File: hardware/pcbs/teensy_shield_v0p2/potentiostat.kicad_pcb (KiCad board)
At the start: 2 copper layers, 144.8 x 88.9 mm, 28 parts, among them K1 CONN_3, P1 CONN_2, P10 CONN_2, P11 CONN_2, P12 CONN_2, P13 CONN_5X2, P14 CONN_5X2, P15 CONN_2X2, P16 CONN_2X2, P17 CONN_2, P18 CONN_2, P19 CONN_2, P2 CONN_2, P20 CONN_2, P21 CONN_2, P3 CONN_2, P4 CONN_2, P5 CONN_2, P6 CONN_2, P7 CONN_2, P8 CONN_2, P9 CONN_2, U2 TEENSY3.1, U6 MEA1D05XXSC

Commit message: Work on layout of teensy pcb version 0.2
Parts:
- added C1: 4.7uF, Capacitor_SMD:C_0603_1608Metric, F.Cu at (-25.4, 90.7)
- added C10: 0.1uF, Capacitor_SMD:C_0603_1608Metric, F.Cu at (-20.9, 74.2)
- added C11: 0.1uF, Capacitor_SMD:C_0603_1608Metric, F.Cu at (-42.3, 100.0)
- added C12: 0.1uF, Capacitor_SMD:C_0603_1608Metric, F.Cu at (-16.9, 74.2)
- added C13: 0.1uF, Capacitor_SMD:C_0603_1608Metric, F.Cu at (-52.5, 110.0)
- added C14: 0.1uF, Capacitor_SMD:C_0603_1608Metric, F.Cu at (-37.8, 93.5)
- added C15: 0.1uF, Capacitor_SMD:C_0603_1608Metric, F.Cu at (-46.3, 100.0)
- added C16: 0.1uF, Capacitor_SMD:C_0603_1608Metric, F.Cu at (-24.9, 80.6)
- added C17: 0.1uF, Capacitor_SMD:C_0603_1608Metric, F.Cu at (-20.9, 76.7)
- added C18: 0.1uF, Capacitor_SMD:C_0603_1608Metric, F.Cu at (-46.3, 102.5)
- added C19: 0.1uF, Capacitor_SMD:C_0603_1608Metric, F.Cu at (-56.5, 110.0)
- added C2: 0.1uF, Capacitor_SMD:C_0603_1608Metric, F.Cu at (160.9, 105.7)
- added C20: 0.1uF, Capacitor_SMD:C_0603_1608Metric, F.Cu at (-21.8, 99.3)
- added C21: 0.1uF, Capacitor_SMD:C_0603_1608Metric, F.Cu at (-26.2, 100.7)
- added C22: 1uF, Capacitor_SMD:C_0603_1608Metric, F.Cu at (71.5, 59.3)
- added C23: 1uF, Capacitor_SMD:C_0603_1608Metric, F.Cu at (77.0, 59.3)
- added C24: 0.1uF, Capacitor_SMD:C_0603_1608Metric, F.Cu at (65.0, 59.2)
- added C25: 56nF, Capacitor_SMD:C_0603_1608Metric, F.Cu at (-13.4, 89.2)
- added C26: 56nF, Capacitor_SMD:C_0603_1608Metric, F.Cu at (-21.8, 96.8)
- added C27: 56nF, Capacitor_SMD:C_0603_1608Metric, F.Cu at (-32.5, 108.6)
- added C28: 56nF, Capacitor_SMD:C_0603_1608Metric, F.Cu at (-26.2, 103.2)
- added C29: 10nF, Capacitor_SMD:C_0603_1608Metric, F.Cu at (-29.4, 85.2)
- added C3: 0.1uF, Capacitor_SMD:C_0603_1608Metric, F.Cu at (172.7, 105.5)
- added C30: 12nF, Capacitor_SMD:C_0603_1608Metric, F.Cu at (-25.4, 85.6)
- added C31: 0.1uF, Capacitor_SMD:C_0603_1608Metric, F.Cu at (-29.4, 90.2)
- added C32: 0.1uF, Capacitor_SMD:C_0603_1608Metric, F.Cu at (-37.8, 98.5)
- added C33: 0.1uF, Capacitor_SMD:C_0603_1608Metric, F.Cu at (147.2, 119.3)
- added C34: 0.1uF, Capacitor_SMD:C_0603_1608Metric, F.Cu at (139.8, 106.9)
- added C35: 0.1uF, Capacitor_SMD:C_0603_1608Metric, F.Cu at (-16.9, 79.2)
- added C36: 0.1uF, Capacitor_SMD:C_0603_1608Metric, F.Cu at (-33.8, 96.0)
- added C37: 0.1uF, Capacitor_SMD:C_0603_1608Metric, F.Cu at (158.0, 118.2)
- added C38: 0.1uF, Capacitor_SMD:C_0603_1608Metric, F.Cu at (149.7, 102.5)
- added C39: 0.1uF, Capacitor_SMD:C_0603_1608Metric, F.Cu at (-29.4, 92.7)
- added C4: 0.1uF, Capacitor_SMD:C_0603_1608Metric, F.Cu at (172.7, 107.2)
- added C40: 0.1uF, Capacitor_SMD:C_0603_1608Metric, F.Cu at (-25.4, 88.1)
- added C41: 0.1uF, Capacitor_SMD:C_0603_1608Metric, F.Cu at (158.0, 119.9)
- added C42: 0.1uF, Capacitor_SMD:C_0603_1608Metric, F.Cu at (-44.5, 107.5)
- added C43: 0.1uF, Capacitor_SMD:C_0603_1608Metric, F.Cu at (-24.9, 83.1)
- added C44: 0.1uF, Capacitor_SMD:C_0603_1608Metric, F.Cu at (-38.3, 103.6)
- added C45: 0.1uF, Capacitor_SMD:C_0603_1608Metric, F.Cu at (-33.8, 98.5)
- added C46: 0.1uF, Capacitor_SMD:C_0603_1608Metric, F.Cu at (-16.9, 81.7)
- added C47: 0.1uF, Capacitor_SMD:C_0603_1608Metric, F.Cu at (-8.92, 74.2)
- added C48: 0.1uF, Capacitor_SMD:C_0603_1608Metric, F.Cu at (-44.5, 110.0)
- added C49: 1uF, Capacitor_SMD:C_0603_1608Metric, F.Cu at (-21.4, 86.7)
- added C5: 4.7uF, Capacitor_SMD:C_0603_1608Metric, F.Cu at (-33.8, 93.5)
- added C50: 0.1uF, Capacitor_SMD:C_0603_1608Metric, F.Cu at (-29.8, 95.2)
- added C51: 1uF, Capacitor_SMD:C_0603_1608Metric, F.Cu at (-12.9, 79.2)
- added C52: 0.1uF, Capacitor_SMD:C_0603_1608Metric, F.Cu at (-34.3, 101.0)
- added C53: 0.1uF, Capacitor_SMD:C_0603_1608Metric, F.Cu at (-3.19, 132.2)
- added C54: 0.1uF, Capacitor_SMD:C_0603_1608Metric, F.Cu at (-3.19, 134.7)
- added C55: 0.1uF, Capacitor_SMD:C_0603_1608Metric, F.Cu at (0.82, 132.2)
- added C6: 3.3nF, Capacitor_SMD:C_0603_1608Metric, F.Cu at (-16.9, 76.7)
- added C7: 2.2uF, Capacitor_SMD:C_0603_1608Metric, F.Cu at (-42.3, 102.5)
- added C8: 2.2uF, Capacitor_SMD:C_0603_1608Metric, F.Cu at (-29.4, 87.7)
- added C9: 2.2uF, Capacitor_SMD:C_0603_1608Metric, F.Cu at (-37.8, 96.0)
- added D1: BAS07-04, Package_TO_SOT_SMD:SOT-23, F.Cu at (-60.7, 109.5)
- added D2: BAS07-04, Package_TO_SOT_SMD:SOT-23, F.Cu at (-29.2, 81.6)
- added P22: Conn_01x02, pin_array:PIN_ARRAY_2X1, F.Cu at (-70.5, 109.1)
- added R1: 12k, Resistor_SMD:R_0603_1608Metric, F.Cu at (-20.9, 84.2)
- added R10: 20k, Resistor_SMD:R_0603_1608Metric, F.Cu at (-25.4, 93.2)
- added R11: 50k, Resistor_SMD:R_0603_1608Metric, F.Cu at (-21.4, 89.2)
- added R12: 100k, Resistor_SMD:R_0603_1608Metric, F.Cu at (-12.9, 81.7)
- added R13: 20k, Resistor_SMD:R_0603_1608Metric, F.Cu at (-29.8, 97.7)
- added R14: 300k, Resistor_SMD:R_0603_1608Metric, F.Cu at (-34.3, 103.6)
- added R15: 30k, Resistor_SMD:R_0603_1608Metric, F.Cu at (-40.5, 110.0)
- added R16: 3k, Resistor_SMD:R_0603_1608Metric, F.Cu at (-17.4, 94.2)
- added R17: 300, Resistor_SMD:R_0603_1608Metric, F.Cu at (-8.91, 79.2)
- added R18: 10k, Resistor_SMD:R_0603_1608Metric, F.Cu at (-30.3, 101.0)
- added R19: 10k, Resistor_SMD:R_0603_1608Metric, F.Cu at (-8.92, 76.7)
- added R2: 12k, Resistor_SMD:R_0603_1608Metric, F.Cu at (-22.2, 101.8)
- added R20: 100k, Resistor_SMD:R_0603_1608Metric, F.Cu at (-25.8, 95.7)
- added R21: 100k, Resistor_SMD:R_0603_1608Metric, F.Cu at (-12.9, 84.2)
- added R22: 50k, Resistor_SMD:R_0603_1608Metric, F.Cu at (-36.5, 106.1)
- added R23: 20k, Resistor_SMD:R_0603_1608Metric, F.Cu at (-17.4, 89.2)
- added R24: 10k, Resistor_SMD:R_0603_1608Metric, F.Cu at (-8.91, 81.7)
- added R25: 20k, Resistor_SMD:R_0603_1608Metric, F.Cu at (-36.5, 108.6)
- added R26: 12k, Resistor_SMD:R_0603_1608Metric, F.Cu at (-25.8, 98.2)
- added R27: 10k, Resistor_SMD:R_0603_1608Metric, F.Cu at (-30.3, 103.6)
- added R28: 12k, Resistor_SMD:R_0603_1608Metric, F.Cu at (-21.4, 94.2)
- added R29: 20k, Resistor_SMD:R_0603_1608Metric, F.Cu at (-13.4, 86.7)
- added R3: 20k, Resistor_SMD:R_0603_1608Metric, F.Cu at (-13.4, 94.2)
- added R30: 1k, Resistor_SMD:R_0603_1608Metric, F.Cu at (-17.4, 86.7)
- added R31: 100, Resistor_SMD:R_0603_1608Metric, F.Cu at (-9.35, 86.7)
- added R32: 4.7k, Resistor_SMD:R_0603_1608Metric, F.Cu at (-28.4, 106.1)
- added R33: 20k, Resistor_SMD:R_0603_1608Metric, F.Cu at (-32.5, 106.1)
- added R34: 12k, Resistor_SMD:R_0603_1608Metric, F.Cu at (-13.4, 91.7)
- added R35: 4.7k, Resistor_SMD:R_0603_1608Metric, F.Cu at (-32.5, 111.1)
- added R36: 12k, Resistor_SMD:R_0603_1608Metric, F.Cu at (-17.8, 96.8)
- added R37: 1k, Resistor_SMD:R_0603_1608Metric, F.Cu at (-9.35, 89.2)
- added R38: 100, Resistor_SMD:R_0603_1608Metric, F.Cu at (-28.4, 108.6)
- added R4: 100k, Resistor_SMD:R_0603_1608Metric, F.Cu at (-5.34, 86.7)
- added R5: 20k, Resistor_SMD:R_0603_1608Metric, F.Cu at (-24.4, 105.7)
- added R6: 20k, Resistor_SMD:R_0603_1608Metric, F.Cu at (-17.8, 99.3)
- added R7: 10k, Resistor_SMD:R_0603_1608Metric, F.Cu at (-21.4, 91.7)
- added R8: 20k, Resistor_SMD:R_0603_1608Metric, F.Cu at (-16.9, 84.2)
- added R9: 10k, Resistor_SMD:R_0603_1608Metric, F.Cu at (-40.5, 107.5)
- added U1: 74HC138, Package_SO:SOIC-16_3.9x9.9mm_P1.27mm, F.Cu at (-69.4, 90.1)
- added U10: REF33XX, Package_TO_SOT_SMD:SOT-23, F.Cu at (-65.2, 109.5)
- added U11: OP07, Package_SO:SOIC-8_3.9x4.9mm_P1.27mm, F.Cu at (-35.6, 89.0)
- added U12: OP07, Package_SO:SOIC-8_3.9x4.9mm_P1.27mm, F.Cu at (-44.1, 95.5)
- added U13: OP07, Package_SO:SOIC-8_3.9x4.9mm_P1.27mm, F.Cu at (-52.5, 105.5)
- added U14: OP07, Package_SO:SOIC-8_3.9x4.9mm_P1.27mm, F.Cu at (-27.2, 76.1)
- added U15: OP07, Package_SO:SOIC-8_3.9x4.9mm_P1.27mm, F.Cu at (-35.6, 82.6)
- added U16: OP07, Package_SO:SOIC-8_3.9x4.9mm_P1.27mm, F.Cu at (-44.1, 89.0)
- added U17: OP07, Package_SO:SOIC-8_3.9x4.9mm_P1.27mm, F.Cu at (-52.5, 99.0)
- added U18: OP07, Package_SO:SOIC-8_3.9x4.9mm_P1.27mm, F.Cu at (-44.1, 76.1)
- added U19: 74HC138, Package_SO:SOIC-16_3.9x9.9mm_P1.27mm, F.Cu at (-69.4, 78.6)
- added U20: OP07, Package_SO:SOIC-8_3.9x4.9mm_P1.27mm, F.Cu at (-44.1, 82.6)
- added U21: 74HC138, Package_SO:SOIC-16_3.9x9.9mm_P1.27mm, F.Cu at (-61.0, 101.5)
- added U3: DG411xY, Package_SO:SOIC-16_3.9x9.9mm_P1.27mm, F.Cu at (-61.0, 78.6)
- added U4: DG411xY, Package_SO:SOIC-16_3.9x9.9mm_P1.27mm, F.Cu at (166.6, 106.3)
- added U5: DG411xY, Package_SO:SOIC-16_3.9x9.9mm_P1.27mm, F.Cu at (-52.5, 78.6)
- added U7: DG411xY, Package_SO:SOIC-16_3.9x9.9mm_P1.27mm, F.Cu at (152.1, 119.1)
- added U8: DG411xY, Package_SO:SOIC-16_3.9x9.9mm_P1.27mm, F.Cu at (138.6, 119.1)
- added U9: TL072, Package_SO:SOIC-8_3.9x4.9mm_P1.27mm, F.Cu at (144.9, 105.4)
- K1: value CONN_3 -> Conn_01x03
- P1, P10, P11, P12, P17, P18, P19, P2, P20, P21, P3, P4, P5, P6, P7, P8, P9: value CONN_2 -> Conn_01x02
- P13, P14: value CONN_5X2 -> Conn_02x05_Odd_Even
- P15, P16: value CONN_2X2 -> Conn_02x02_Odd_Even
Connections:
- net /+12V renamed /+15V
- net /-12V renamed /-15V
- net /REF_10V renamed /REF_NEG_0V6
- net /REF_ELECT renamed /REF_ELECT_OUT
- net /RX renamed /D4
- net /TIA_SW1_IN1 renamed Net-(U2-Pad4)
- net /TIA_SW2_IN3 renamed Net-(U2-Pad29)
- net /TIA_SW2_IN4 renamed Net-(U2-Pad30)
- net /TX renamed /D3
- net /WRK_ELECT renamed /WRK_ELECT_OUT
- K1 pad 1: /CTR_ELECT -> /CTR_ELECT_OUT
- P1 pad 1: /CTR_ELECT -> /CTR_ELECT_OUT
- U2 pad 10: /TIA_SW2_IN1 -> /SW_REF_ELECT
- U2 pad 11: /TIA_SW2_IN2 -> /SW_WRK_ELECT
- U2 pad 15: (no net) -> Net-(U2-Pad15)
- U2 pad 18: (no net) -> Net-(U2-Pad18)
- U2 pad 21: (no net) -> Net-(U2-Pad21)
- U2 pad 24: (no net) -> Net-(U2-Pad24)
- U2 pad 27: (no net) -> /REF_GAIN_A0
- U2 pad 28: (no net) -> /REF_GAIN_A1
- U2 pad 31: (no net) -> Net-(U2-Pad31)
- U2 pad 34: (no net) -> Net-(U2-Pad34)
- U2 pad 35: (no net) -> Net-(U2-Pad35)
- U2 pad 44: (no net) -> Net-(U2-Pad44)
- U2 pad 45: (no net) -> Net-(U2-Pad45)
- U2 pad 46: (no net) -> Net-(U2-Pad46)
- U2 pad 47: (no net) -> Net-(U2-Pad47)
- U2 pad 48: (no net) -> Net-(U2-Pad48)
- U2 pad 49: (no net) -> Net-(U2-Pad49)
- U2 pad 50: (no net) -> Net-(U2-Pad50)
- U2 pad 51: (no net) -> Net-(U2-Pad51)
- U2 pad 7: /TIA_SW1_IN2 -> /TIA_GAIN_A0
- U2 pad 8: /TIA_SW1_IN3 -> /TIA_GAIN_A1
- U2 pad 9: /TIA_SW1_IN4 -> /SW_CTR_ELECT

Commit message: Finished initial layout for version 0.2 of teensy pcb.
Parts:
- removed C49, C51: 1uF, Capacitor_SMD:C_0603_1608Metric
- moved U5 220.0 mm to (167.3, 69.2)
- moved P22 212.9 mm to (140.7, 135.6), turned to 270 degrees
- moved U16 211.9 mm to (167.6, 81.0)
- moved C45 208.9 mm to (174.2, 80.4)
- moved U3 206.6 mm to (145.5, 72.6), turned to 270 degrees
- moved U15 203.5 mm to (167.6, 91.7)
- moved C40 200.3 mm to (174.1, 70.2)
- moved R22 200.2 mm to (160.7, 71.1), turned to 180 degrees
- moved C13 199.5 mm to (144.7, 79.4), turned to 270 degrees
- moved C29 199.4 mm to (169.7, 96.0), turned to 180 degrees
- moved C43 199.2 mm to (174.1, 91.1)
- moved C32 199.1 mm to (161.2, 93.6), turned to 180 degrees
- moved C36 195.3 mm to (161.0, 82.9), turned to 180 degrees
- moved C19 195.1 mm to (133.7, 66.5)
- moved U17 194.5 mm to (141.9, 93.0)
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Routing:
- net /+15V: track 0.00 -> 53.0 mm
- net /-15V: track 0.00 -> 51.0 mm
- net /3V3: track 0.00 -> 29.2 mm
- net /AGND: track 0.00 -> 12.9 mm
- net /REF_3V: track 0.00 -> 12.3 mm
- net Net-(C6-Pad2): track 0.00 -> 6.23 mm
- net Net-(C29-Pad2): track 0.00 -> 5.59 mm
- net /GND: track 0.00 -> 5.39 mm
- net Net-(C25-Pad1): track 0.00 -> 5.37 mm
- net Net-(R25-Pad1): track 0.00 -> 5.34 mm
- net /5V: track 0.00 -> 5.18 mm
- net Net-(D2-Pad3): track 0.00 -> 4.68 mm
- net Net-(D1-Pad3): track 0.00 -> 4.25 mm
- net Net-(C26-Pad1): track 0.00 -> 4.03 mm
- net Net-(R23-Pad1): track 0.00 -> 3.69 mm
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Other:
- net class Power: trace_width 0.508 -> 0.381
- board text added: "+0.6V"
- board text added: "+15V"
- board text added: "-0.6V"
- board text added: "-15V"
- board text added: "BIP"
- board text added: "BIP NX"
- board text added: "BUF"
- board text added: "CTR-E"
- board text added: "DAC"
- board text added: "REF-E"
- board text added: "TIA"
- board text added: "UNI"
- board text removed: "+12V"
- board text removed: "-12V"
- board text removed: "CTR E"
- board text removed: "DAC BIP"
- board text removed: "DAC BIP NX"
- board text removed: "DAC UNI"
- board text removed: "REF 0.6V"
- board text removed: "REF 10V"
- board text removed: "REF E BUF"
- board text removed: "REF E UNI"
- board text removed: "TIA BIP"
- board text removed: "TIA UNI"

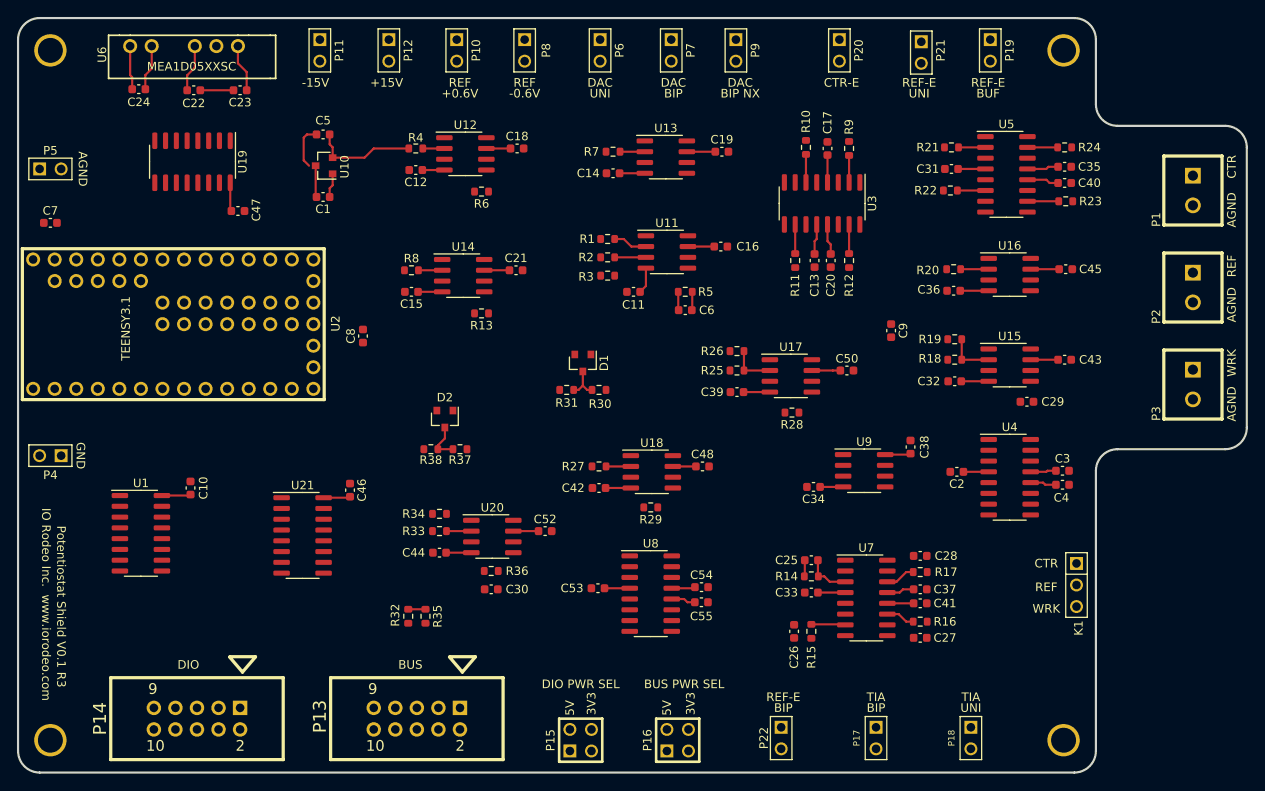
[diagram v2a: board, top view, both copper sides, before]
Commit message: Completed initial routing of PCB.
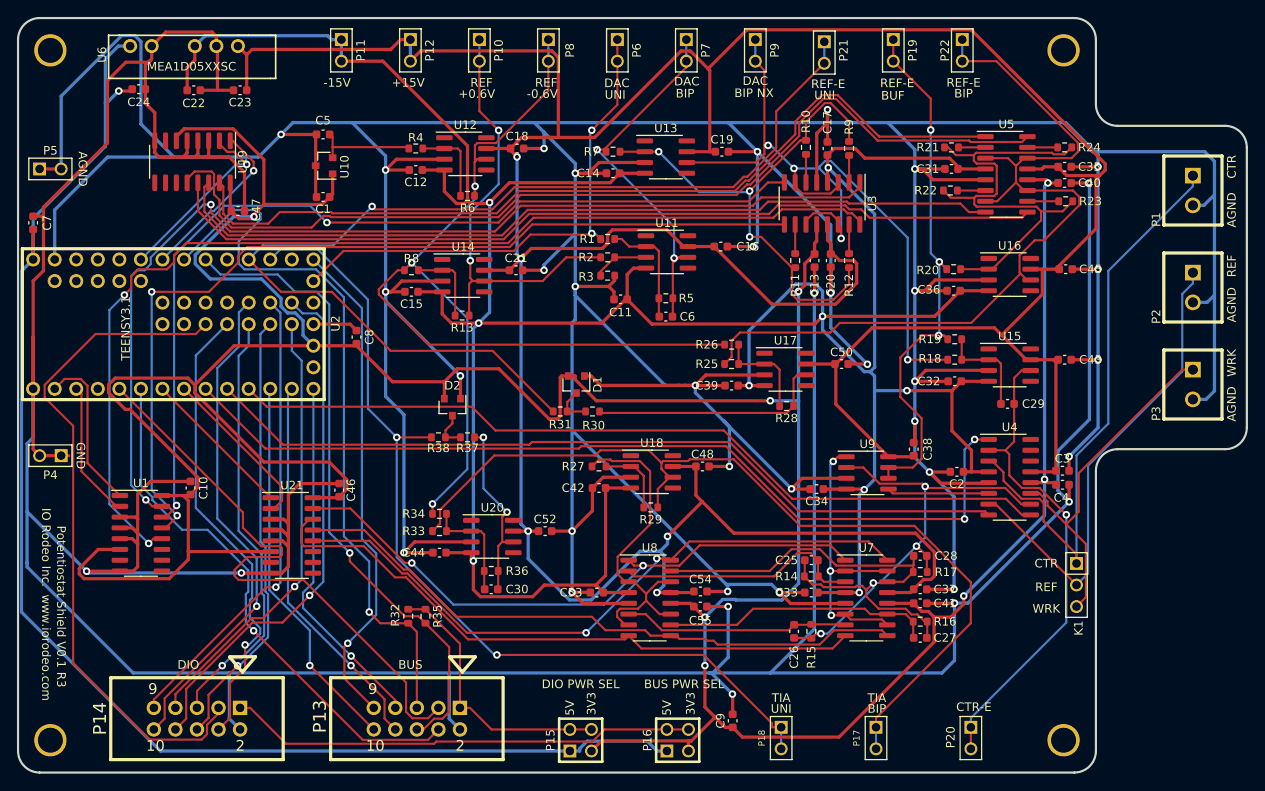
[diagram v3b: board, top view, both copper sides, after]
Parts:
- moved P22 83.8 mm to (162.1, 54.6)
- moved P20 82.5 mm to (163.1, 135.6)
- moved C9 49.6 mm to (135.0, 133.6), turned to 90 degrees
- moved P18 22.4 mm to (140.7, 135.6)
- moved P19 11.4 mm to (153.9, 54.6)
- moved P21 11.4 mm to (145.8, 54.9)
- moved P8 2.79 mm to (113.3, 54.6)
- moved P10 2.67 mm to (105.2, 54.6)
- moved D1 2.65 mm to (116.6, 94.0)
- moved R30 2.65 mm to (118.5, 97.2)
- moved R31 2.65 mm to (114.7, 97.2)
- moved P11 2.54 mm to (88.9, 54.6)
- moved P12 2.54 mm to (97.0, 54.6)
- moved C6 2.41 mm to (127.1, 86.0)
- moved R5 2.41 mm to (127.1, 83.8)
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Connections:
- C22 pad 2: /AGND -> /GND
- C23 pad 2: /AGND -> /GND
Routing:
- net /AGND: track 12.9 -> 812.0 mm, vias 0 -> 31
- net /GND: track 5.39 -> 500.0 mm, vias 0 -> 8
- net /3V3: track 29.2 -> 448.0 mm, vias 0 -> 8
- net /+15V: track 53.0 -> 455.3 mm, vias 0 -> 5
- net /-15V: track 51.0 -> 394.6 mm, vias 0 -> 9
- net /5V: track 5.18 -> 164.1 mm, vias 0 -> 1
- net /SW_GAIN_10X: track 0.00 -> 126.8 mm, vias 0 -> 2
- net /REF_ELECT_UNI: track 0.00 -> 126.0 mm, vias 0 -> 1
- net /SW_GAIN_1X: track 0.00 -> 123.7 mm, vias 0 -> 2
- net /REF_NEG_0V6: track 0.00 -> 119.9 mm, vias 0 -> 3
- net /SW_GAIN_INV_10X: track 0.00 -> 114.7 mm
- net /SW_GAIN_2X: track 0.00 -> 109.0 mm, vias 0 -> 2
- net /SW_GAIN_5X: track 0.00 -> 108.3 mm, vias 0 -> 2
- net /SW_CTR_ELECT: track 0.00 -> 107.5 mm, vias 0 -> 2
- net /TIA_OUT_UNI: track 0.00 -> 106.7 mm, vias 0 -> 2
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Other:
- board text added: "Maybe move REF-E BIP to other side of board. Also move CTR-E to this side ... maybe at the top?"

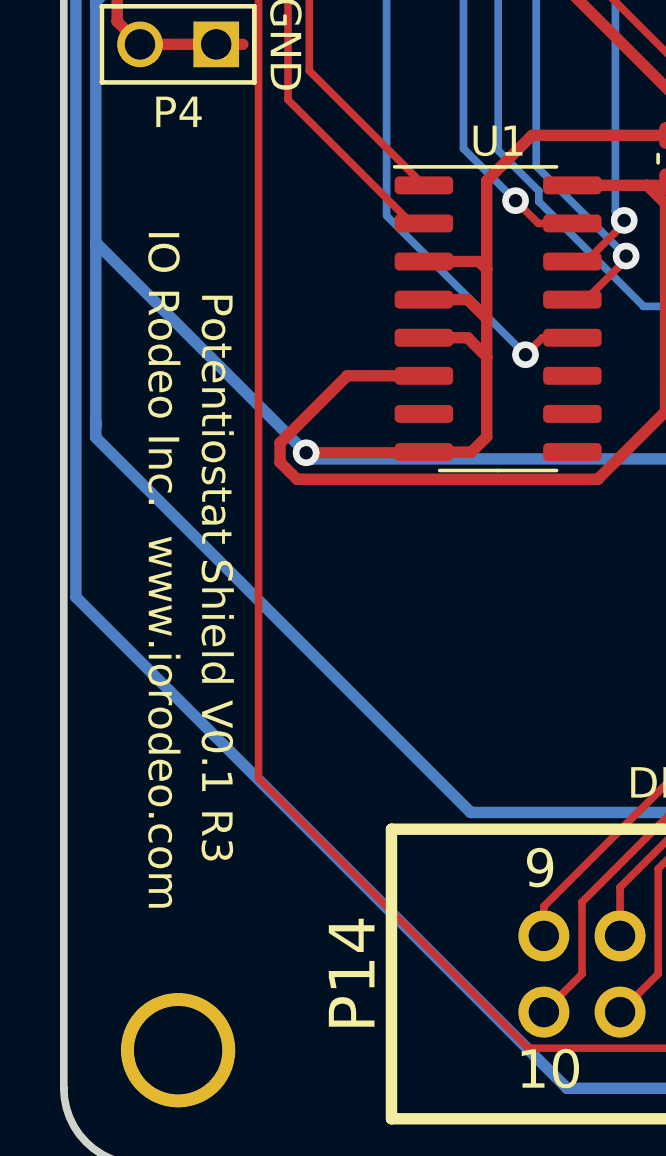
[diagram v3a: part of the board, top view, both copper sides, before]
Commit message: Added gerber files for new version.  Added cpl file for assembly.
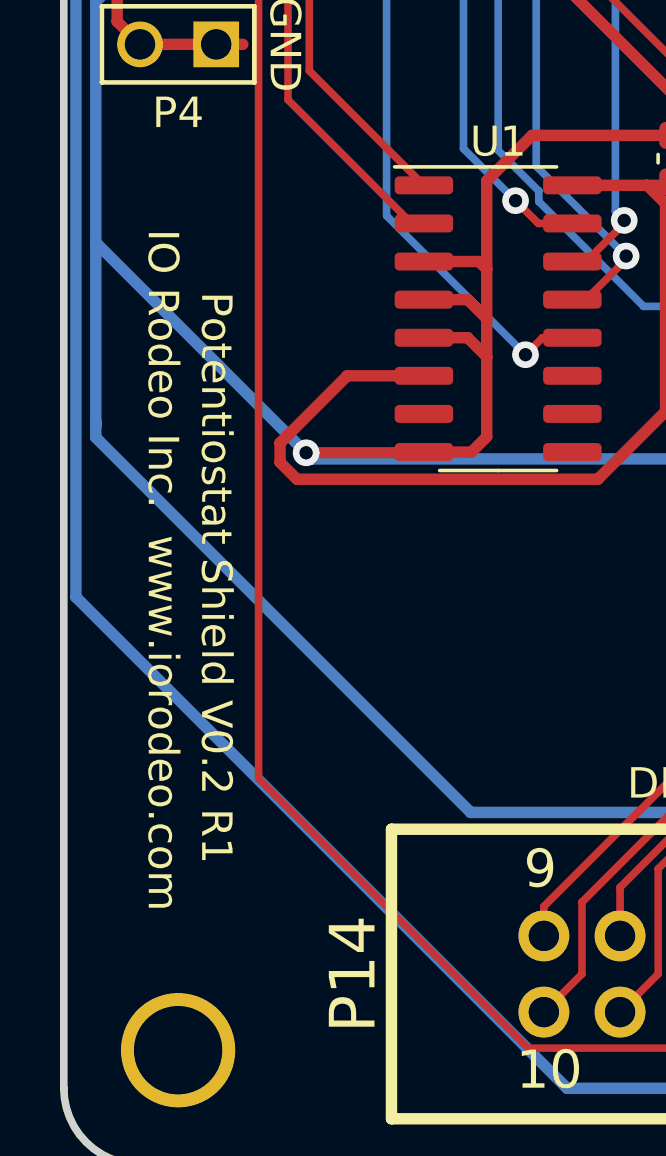
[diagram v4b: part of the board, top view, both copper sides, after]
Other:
- board text added: "Potentiostat Shield V0.2 R1"
- board text removed: "Potentiostat Shield V0.1 R3"

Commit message: Modified R33 resistor value which caused gain error, for transimpedance amplifier in first prototypes of V0.2 design.
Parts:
- C25, C26, C27, C28: value 56nF -> 68nF
- R33: value 20k -> 12k
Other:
- board text removed: "Maybe move REF-E BIP to other side of board. Also move CTR-E to this side ... maybe at the top?"
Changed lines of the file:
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@@
   (general
     (thickness 1.6)
-    (drawings 64)
+    (drawings 63)
     (tracks 1751)
     (zones 0)
@@
     (pad_to_mask_clearance 0)
     (aux_axis_origin 0 0)
-    (visible_elements FFFFFFBF)
+    (visible_elements FFFFEFBF)
     (pcbplotparams
       (layerselection 0x010fc_ffffffff)
@@
       (effects (font (size 1 1) (thickness 0.15)))
     )
-    (fp_text value 56nF (at 0 1.43) (layer F.Fab)
+    (fp_text value 68nF (at 0 1.43) (layer F.Fab)
       (effects (font (size 1 1) (thickness 0.15)))
     )
@@
       (effects (font (size 1 1) (thickness 0.15)))
     )
-    (fp_text value 56nF (at 0 1.43 90) (layer F.Fab)
+    (fp_text value 68nF (at 0 1.43 90) (layer F.Fab)
       (effects (font (size 1 1) (thickness 0.15)))
     )
@@
       (effects (font (size 1 1) (thickness 0.15)))
     )
-    (fp_text value 56nF (at 0 1.43) (layer F.Fab)
+    (fp_text value 68nF (at 0 1.43) (layer F.Fab)
       (effects (font (size 1 1) (thickness 0.15)))
     )
@@
       (effects (font (size 1 1) (thickness 0.15)))
     )
-    (fp_text value 56nF (at 0 1.43) (layer F.Fab)
+    (fp_text value 68nF (at 0 1.43) (layer F.Fab)
       (effects (font (size 1 1) (thickness 0.15)))
     )
@@
       (effects (font (size 1 1) (thickness 0.15)))
     )
-    (fp_text value 20k (at 0 1.43) (layer F.Fab)
+    (fp_text value 12k (at 0 1.43) (layer F.Fab)
       (effects (font (size 1 1) (thickness 0.15)))
     )
@@
     )
   )
-  (gr_text "Maybe move REF-E BIP to other side of board. \nAlso move CTR-E to this side ... maybe at the top?" (at 142.9004 142.1384) (layer Dwgs.User)
-    (effects (font (size 1 1) (thickness 0.15)))
-  )
   (gr_text "IO Rodeo Inc.  www.iorodeo.com" (at 54.102 119.888 270) (layer F.SilkS)
